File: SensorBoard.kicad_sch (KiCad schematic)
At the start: 16 parts, among them J1 Conn_02x04_Odd_Even, U1 TCRT5000, U2 TCRT5000, U3 TCRT5000, U4 TCRT5000, U5 TCRT5000

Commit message: Add files via upload
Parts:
- J1: footprint (none) -> Connector_PinHeader_2.54mm:PinHeader_2x04_P2.54mm_Vertical
- R1, R10, R2, R3, R4, R5, R6, R7, R8, R9: footprint (none) -> Resistor_SMD:R_0805_2012Metric
- U1, U2, U3, U4, U5: footprint TCRT5000:OPTO_TCRT5000 -> kicad_mod:OPTO_TCRT5000
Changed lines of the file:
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@@
       (effects (font (size 1.27 1.27)) (justify left))
     )
-    (property "Footprint" "" (at 154.432 69.85 90)
+    (property "Footprint" "Resistor_SMD:R_0805_2012Metric" (at 154.432 69.85 90)
       (effects (font (size 1.27 1.27)) hide)
     )
@@
       (effects (font (size 1.27 1.27)))
     )
-    (property "Footprint" "TCRT5000:OPTO_TCRT5000" (at 39.37 38.1 0)
+    (property "Footprint" "kicad_mod:OPTO_TCRT5000" (at 39.37 38.1 0)
       (effects (font (size 1.27 1.27)) (justify bottom) hide)
     )
@@
       (effects (font (size 1.27 1.27)) (justify left))
     )
-    (property "Footprint" "" (at 29.972 52.07 90)
+    (property "Footprint" "Resistor_SMD:R_0805_2012Metric" (at 29.972 52.07 90)
       (effects (font (size 1.27 1.27)) hide)
     )
@@
       (effects (font (size 1.27 1.27)))
     )
-    (property "Footprint" "TCRT5000:OPTO_TCRT5000" (at 163.83 123.19 0)
+    (property "Footprint" "kicad_mod:OPTO_TCRT5000" (at 163.83 123.19 0)
       (effects (font (size 1.27 1.27)) (justify bottom) hide)
     )
@@
       (effects (font (size 1.27 1.27)) (justify left))
     )
-    (property "Footprint" "" (at 31.242 161.29 90)
+    (property "Footprint" "Resistor_SMD:R_0805_2012Metric" (at 31.242 161.29 90)
       (effects (font (size 1.27 1.27)) hide)
     )
@@
       (effects (font (size 1.27 1.27)) (justify left))
     )
-    (property "Footprint" "" (at 46.482 161.29 90)
+    (property "Footprint" "Resistor_SMD:R_0805_2012Metric" (at 46.482 161.29 90)
       (effects (font (size 1.27 1.27)) hide)
     )
@@
       (effects (font (size 1.27 1.27)) (justify left))
     )
-    (property "Footprint" "" (at 154.432 137.16 90)
+    (property "Footprint" "Resistor_SMD:R_0805_2012Metric" (at 154.432 137.16 90)
       (effects (font (size 1.27 1.27)) hide)
     )
@@
       (effects (font (size 1.27 1.27)))
     )
-    (property "Footprint" "TCRT5000:OPTO_TCRT5000" (at 40.64 96.52 0)
+    (property "Footprint" "kicad_mod:OPTO_TCRT5000" (at 40.64 96.52 0)
       (effects (font (size 1.27 1.27)) (justify bottom) hide)
     )
@@
       (effects (font (size 1.27 1.27)))
     )
-    (property "Footprint" "TCRT5000:OPTO_TCRT5000" (at 40.64 147.32 0)
+    (property "Footprint" "kicad_mod:OPTO_TCRT5000" (at 40.64 147.32 0)
       (effects (font (size 1.27 1.27)) (justify bottom) hide)
     )
@@
       (effects (font (size 1.27 1.27)) (justify left))
     )
-    (property "Footprint" "" (at 169.672 69.85 90)
+    (property "Footprint" "Resistor_SMD:R_0805_2012Metric" (at 169.672 69.85 90)
       (effects (font (size 1.27 1.27)) hide)
     )
@@
       (effects (font (size 1.27 1.27)) (justify left))
     )
-    (property "Footprint" "" (at 31.242 110.49 90)
+    (property "Footprint" "Resistor_SMD:R_0805_2012Metric" (at 31.242 110.49 90)
       (effects (font (size 1.27 1.27)) hide)
     )
@@
       (effects (font (size 1.27 1.27)) (justify left))
     )
-    (property "Footprint" "" (at 45.212 52.07 90)
+    (property "Footprint" "Resistor_SMD:R_0805_2012Metric" (at 45.212 52.07 90)
       (effects (font (size 1.27 1.27)) hide)
     )
@@
       (effects (font (size 1.27 1.27)))
     )
-    (property "Footprint" "" (at 111.76 97.79 0)
+    (property "Footprint" "Connector_PinHeader_2.54mm:PinHeader_2x04_P2.54mm_Vertical" (at 111.76 97.79 0)
       (effects (font (size 1.27 1.27)) hide)
     )
@@
       (effects (font (size 1.27 1.27)) (justify left))
     )
-    (property "Footprint" "" (at 46.482 110.49 90)
+    (property "Footprint" "Resistor_SMD:R_0805_2012Metric" (at 46.482 110.49 90)
       (effects (font (size 1.27 1.27)) hide)
     )
@@
       (effects (font (size 1.27 1.27)) (justify left))
     )
-    (property "Footprint" "" (at 169.672 137.16 90)
+    (property "Footprint" "Resistor_SMD:R_0805_2012Metric" (at 169.672 137.16 90)
       (effects (font (size 1.27 1.27)) hide)
     )
@@
       (effects (font (size 1.27 1.27)))
     )
-    (property "Footprint" "TCRT5000:OPTO_TCRT5000" (at 163.83 55.88 0)
-      (effects (font (size 1.27 1.27)) (justify bottom) hide)
-    )
+    (property "Footprint" "kicad_mod:OPTO_TCRT5000" (at 163.83 55.88 0)
+      (effects (font (size 1.27 1.27)) (justify bottom) hide)
+    )

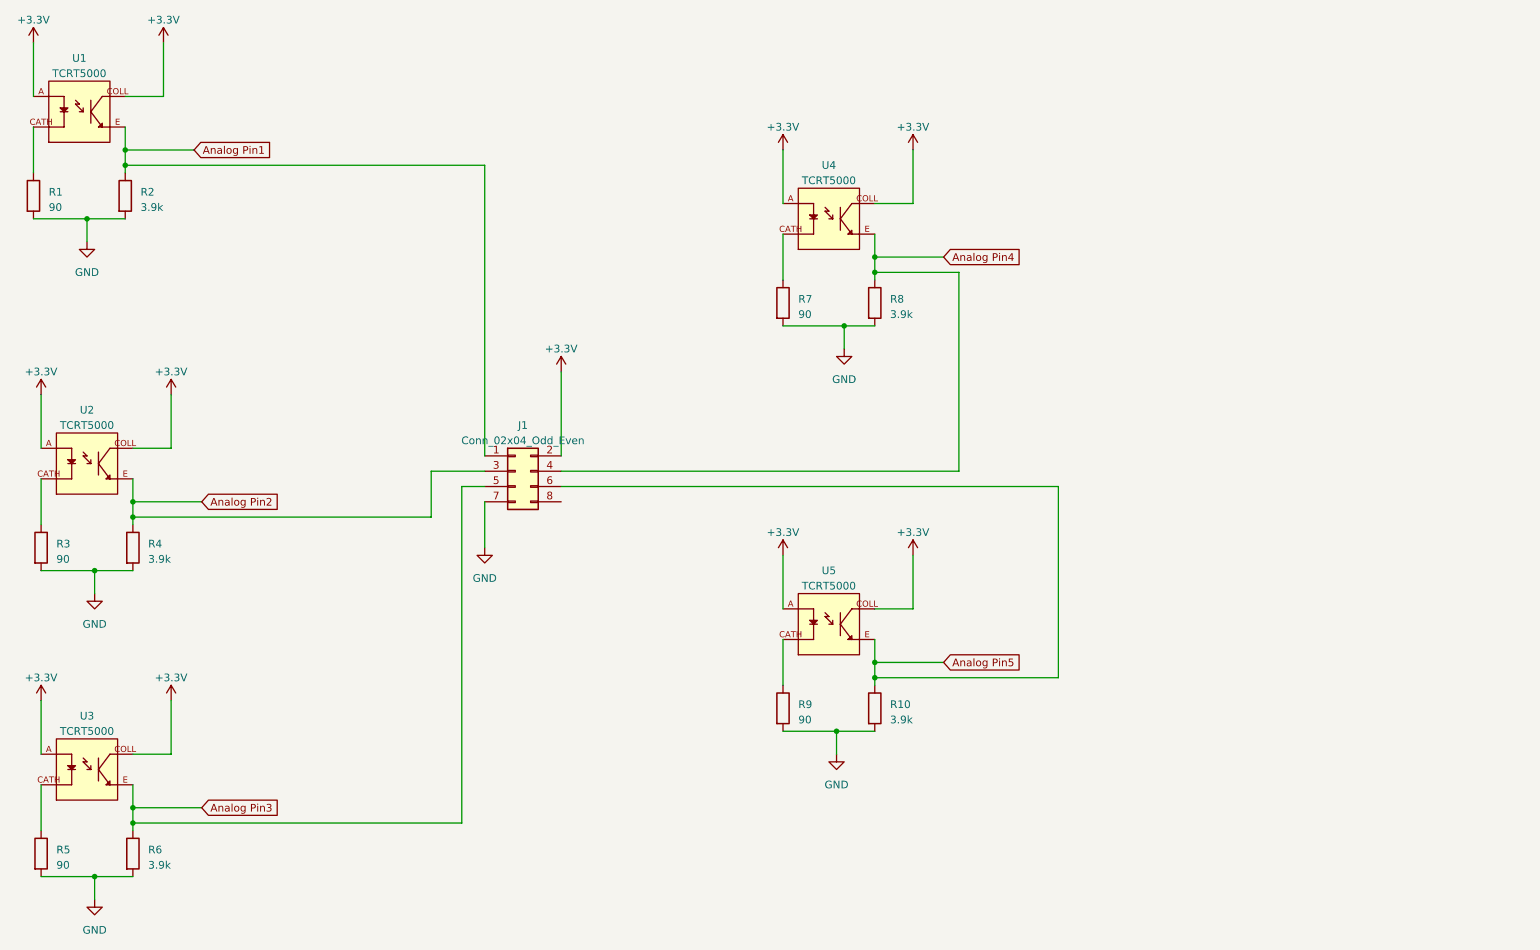
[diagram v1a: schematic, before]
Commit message: Changed Sensor Board
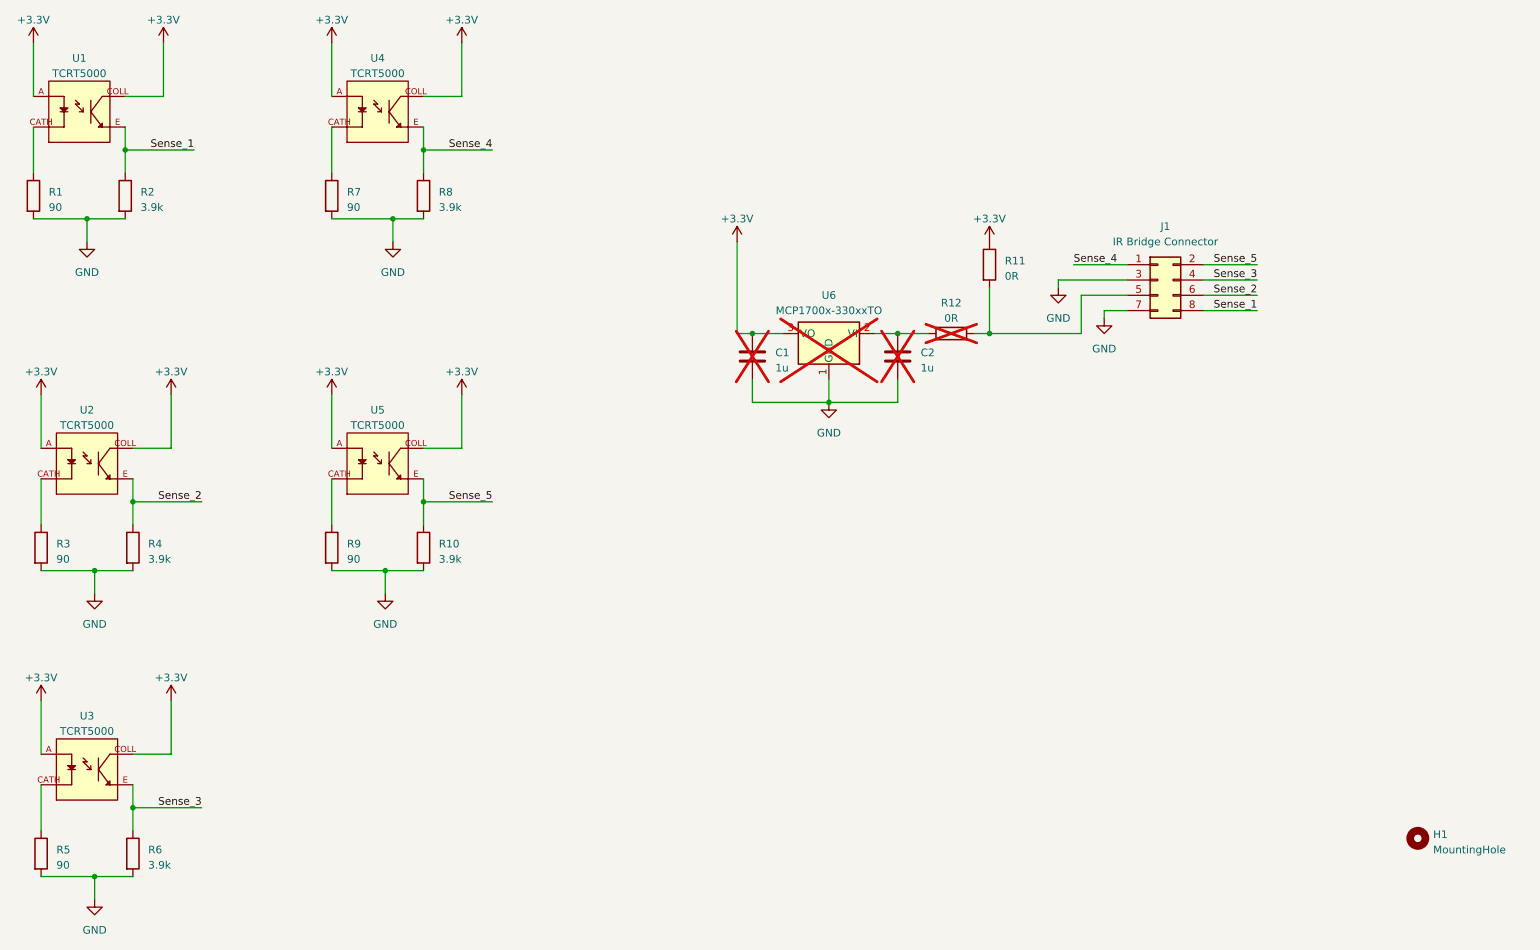
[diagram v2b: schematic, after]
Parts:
- added C1, C2: 1u, Capacitor_SMD:C_0603_1608Metric_Pad1.08x0.95mm_HandSolder, symbol Device:C
- added H1: MountingHole, MountingHole:MountingHole_2.2mm_M2, symbol Mechanical:MountingHole
- added R11, R12: 0R, Resistor_SMD:R_0805_2012Metric, symbol Device:R
- added U6: MCP1700x-330xxTO, Package_TO_SOT_THT:TO-92_Inline, symbol Regulator_Linear:MCP1700x-330xxTO
- J1: value Conn_02x04_Odd_Even -> IR Bridge Connector
- U1, U2, U3, U4, U5: footprint kicad_mod:OPTO_TCRT5000 -> OptoDevice:OPTO_TCRT5000
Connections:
- net +3.3V: now also C1.1, R11.1, U6.3 (VO); no longer J1.2 (Pin_2)
- net GND: now also J1.3 (Pin_3), C1.2, C2.2, U6.1 (GND)
- net Sense_1: now reaches J1.8 (Pin_8)
- net Sense_1: now also R2.1, U1.E
- removed net Analog Pin1: J1.1 (Pin_1), R2.1, U1.E
- net Analog Pin2 renamed Sense_2
- net Sense_2: now also J1.6 (Pin_6); no longer J1.3 (Pin_3)
- net Analog Pin3 renamed Sense_3
- net Sense_3: now also J1.4 (Pin_4); no longer J1.5 (Pin_5)
- net Analog Pin4 renamed Sense_4
- net Sense_4: now also J1.1 (Pin_1); no longer J1.4 (Pin_4)
- net Analog Pin5 renamed Sense_5
- net Sense_5: now also J1.2 (Pin_2); no longer J1.6 (Pin_6)
- new net: J1.5 (Pin_5), R11.2, R12.2
- new net: C2.1, R12.1, U6.2 (VI)
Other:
- moved on the sheet: J1, R10, R7, R8, R9, U4, U5

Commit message: Edits to both boards
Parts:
- added C3, C4, C5, C6, C7: C, Capacitor_SMD:C_1206_3216Metric, symbol Device:C
- added R13, R14, R15, R16, R17: R, Resistor_SMD:R_0805_2012Metric, symbol Device:R
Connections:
- net GND: now also C3.2, C4.2, C5.2, C6.2, C7.2
- net Sense_1: now also C3.1, R13.1, R13.2
- net Sense_2: now also C4.1, R14.1, R14.2
- net Sense_3: now also C5.1, R15.1, R15.2
- net Sense_4: now also C6.1, R16.1, R16.2
- net Sense_5: now also C7.1, R17.1, R17.2
